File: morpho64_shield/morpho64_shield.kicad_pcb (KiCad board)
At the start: 2 copper layers, 70 x 57 mm, 13 parts, among them J1 CN7, J2 CN10, J3 Conn_Coaxial_Small, U1 ADA4505-1ARJZ-R7, U2 ADA4505-1ARJZ-R7, U3 ADA4505-1ARJZ-R7, U4 AP63203WU

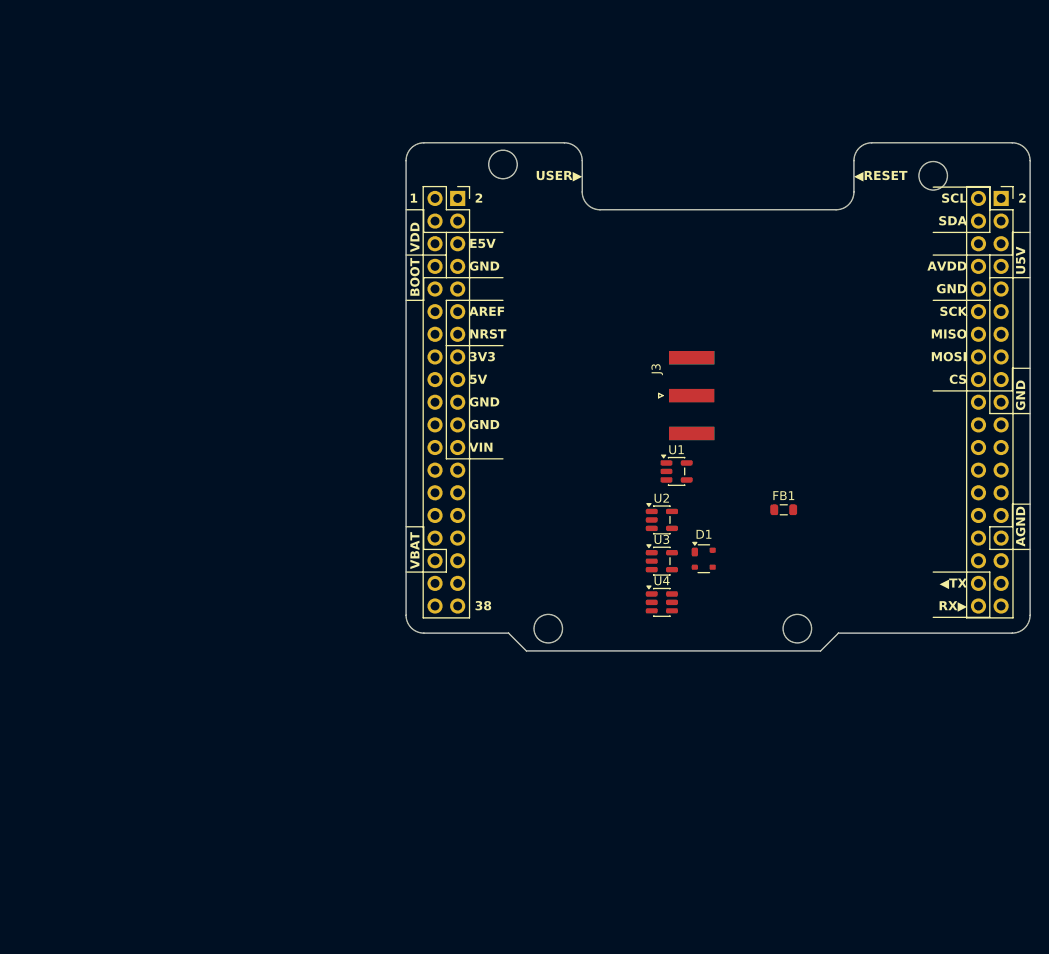
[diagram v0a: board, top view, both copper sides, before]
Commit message: esd + caps
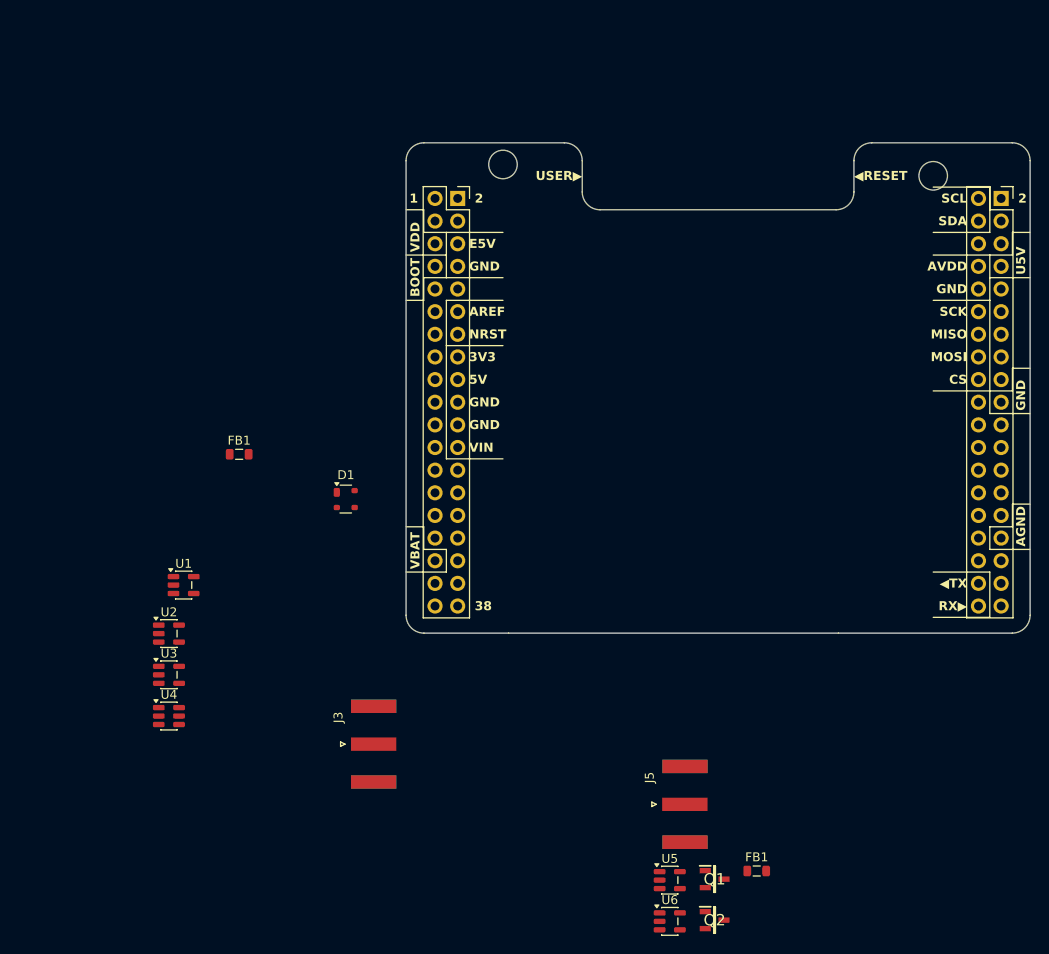
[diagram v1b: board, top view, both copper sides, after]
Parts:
- removed H1, H4: MountingHole, MountingHole:MountingHole_3.2mm_M3_ISO14580
- added FB1: FerriteBead, Inductor_SMD:L_0805_2012Metric, F.Cu at (156.7, 136.4)
- added J5: Conn_Coaxial_Small, Connector_Coaxial:SMA_Amphenol_132289_EdgeMount, F.Cu at (148.7, 128.9)
- added Q1: FMMT493TC, SamacSys_Parts:SOT95P237X112-3N, F.Cu at (152.0, 137.3)
- added Q2: FMMT593TC, SamacSys_Parts:SOT95P237X112-3N, F.Cu at (152.0, 141.9)
- added U5: OPA596DBVR, Package_TO_SOT_SMD:SOT-23-5, F.Cu at (147.0, 137.4)
- added U6: OPA596DBVR, Package_TO_SOT_SMD:SOT-23-5, F.Cu at (147.0, 142.1)
- moved FB1 61.4 mm to (98.7, 89.7)
- moved U1 56.7 mm to (92.5, 104.3)
- moved U2 56.7 mm to (90.8, 109.8)
- moved U3 56.7 mm to (90.8, 114.4)
- moved U4 56.7 mm to (90.8, 119.0)
- moved J3 52.9 mm to (113.8, 122.2)
- moved D1 40.7 mm to (110.6, 94.7)
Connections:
- net Net-(C1-Pad2) renamed /analog_input/IN_U
- net Net-(D1-I/O1) renamed /analog_input/IN_Q
- net Net-(R4-Pad2) renamed /analog_input/ADC2
- net Net-(R6-Pad2) renamed /analog_input/ADC1
- J1 pad 31: unconnected-(J1-Pin_31-Pad31) -> /shield/DAC
- J1 pad 33: unconnected-(J1-Pin_33-Pad33) -> /shield/PB0
- J1 pad 35: unconnected-(J1-Pin_35-Pad35) -> /shield/ADC2
- J1 pad 36: unconnected-(J1-Pin_36-Pad36) -> /shield/ADC2
- J1 pad 37: unconnected-(J1-Pin_37-Pad37) -> /shield/ADC1
- J2 pad 21: unconnected-(J2-Pin_21-Pad21) -> /shield/PB2
- J2 pad 23: unconnected-(J2-Pin_23-Pad23) -> /shield/PB1
- J2 pad 28: unconnected-(J2-Pin_28-Pad28) -> /shield/PB4
- J2 pad 30: unconnected-(J2-Pin_30-Pad30) -> /shield/PB5
- J2 pad 32: unconnected-(J2-Pin_32-Pad32) -> /shield/PB3
- J2 pad 4: unconnected-(J2-Pin_4-Pad4) -> /shield/PB6
- J2 pad 6: unconnected-(J2-Pin_6-Pad6) -> /shield/PB7
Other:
- board size 70 x 57 mm -> 70 x 55 mm

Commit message: First part of layout
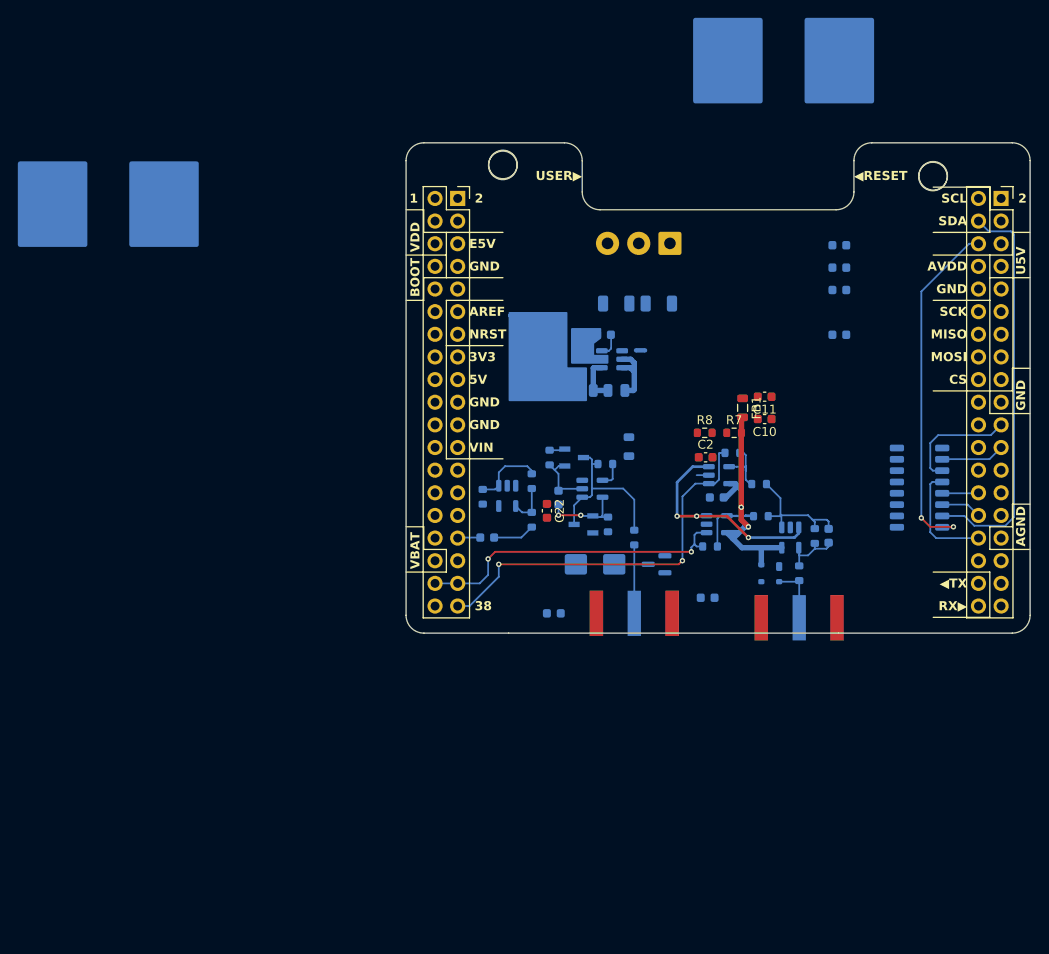
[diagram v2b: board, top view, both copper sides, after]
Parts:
- added C1: C, Capacitor_SMD:C_0603_1608Metric, B.Cu at (164.8, 98.8)
- added C10: 100nF, Capacitor_SMD:C_0603_1608Metric, F.Cu at (157.6, 85.7)
- added C11: 100nF, Capacitor_SMD:C_0603_1608Metric, F.Cu at (157.6, 83.2)
- added C12: C, Capacitor_SMD:C_0603_1608Metric, B.Cu at (126.5, 99.0)
- added C13: 100nF, Capacitor_SMD:C_0603_1608Metric, B.Cu at (166.0, 66.2)
- added C18: 100nF, Capacitor_SMD:C_0603_1608Metric, B.Cu at (166.0, 68.7)
- added C19: 100nF, Capacitor_SMD:C_0603_1608Metric, B.Cu at (166.0, 71.2)
- added C2: 100nF, Capacitor_SMD:C_0603_1608Metric, F.Cu at (151.0, 90.0)
- added C20: 100nF, Capacitor_SMD:C_0603_1608Metric, B.Cu at (152.2, 94.5)
- added C21: 100nF, Capacitor_SMD:C_0603_1608Metric, B.Cu at (166.0, 76.2)
- added C22: 100nF, Capacitor_SMD:C_0603_1608Metric, F.Cu at (133.2, 96.0)
- added C23: DNP, Capacitor_SMD:C_0603_1608Metric, B.Cu at (134.5, 94.5)
- added C24: 100nF, Capacitor_SMD:C_0603_1608Metric, B.Cu at (151.2, 105.8)
- added C25: 100nF, Capacitor_SMD:C_0603_1608Metric, B.Cu at (134.0, 107.5)
- added C3: 22uF, Capacitor_SMD:C_1206_3216Metric, B.Cu at (141.0, 72.8)
- added C4: 22uF, Capacitor_SMD:C_1206_3216Metric, B.Cu at (145.8, 72.8)
- added C5: 470uF, Capacitor_SMD:CP_Elec_16x17.5, B.Cu at (84.0, 61.6)
- added C6: 470uF, Capacitor_SMD:CP_Elec_16x17.5, B.Cu at (159.8, 45.5)
- added C7: 100nF, Capacitor_SMD:C_0603_1608Metric, B.Cu at (139.6, 76.2)
- added C8: 22uF, Capacitor_SMD:C_0805_2012Metric, B.Cu at (137.4, 82.5)
- added C9: 10uF, Capacitor_SMD:C_0805_2012Metric, B.Cu at (141.0, 82.5)
- added D2: SMBJ24CA, Diode_SMD:D_SMB, B.Cu at (138.6, 102.0)
- added D3: BAT54S, Package_TO_SOT_SMD:SOT-23, B.Cu at (145.5, 102.0)
- added H1: MountingHole, MountingHole:MountingHole_3.2mm_M3_ISO14580, B.Cu at (128.2, 57.2)
- added H4: MountingHole, MountingHole:MountingHole_3.2mm_M3_ISO14580, B.Cu at (176.5, 58.5)
- added J4: Screw_Terminal_01x03, TerminalBlock_4Ucon:TerminalBlock_4Ucon_1x03_P3.50mm_Vertical, B.Cu at (147.0, 66.0)
- added L1: 4.7uH, Inductor_SMD:L_7.3x7.3_H4.5, B.Cu at (133.7, 77.5)
- added NT1: NetTie_2, NetTie:NetTie-2_SMD_Pad0.5mm, B.Cu at (143.7, 78.0)
- added R1: R, Resistor_SMD:R_0603_1608Metric, B.Cu at (161.5, 103.0)
- added R10: R, Resistor_SMD:R_0603_1608Metric, B.Cu at (140.1, 97.5)
- added R11: R, Resistor_SMD:R_0603_1608Metric, B.Cu at (126.0, 94.4)
- added R12: R, Resistor_SMD:R_0603_1608Metric, B.Cu at (139.8, 90.8)
- added R13: R, Resistor_SMD:R_0603_1608Metric, B.Cu at (131.5, 97.0)
- added R14: R, Resistor_SMD:R_0603_1608Metric, B.Cu at (131.5, 92.7)
- added R15: DNP, Resistor_SMD:R_0603_1608Metric, B.Cu at (143.0, 99.0)
- added R2: R, Resistor_SMD:R_0603_1608Metric, B.Cu at (163.2, 98.8)
- added R3: R, Resistor_SMD:R_0603_1608Metric, B.Cu at (157.2, 96.6)
- added R4: R, Resistor_SMD:R_0603_1608Metric, B.Cu at (151.5, 100.0)
- added R5: R, Resistor_SMD:R_0603_1608Metric, B.Cu at (157.0, 93.0)
- added R6: R, Resistor_SMD:R_0603_1608Metric, B.Cu at (154.0, 89.5)
- added R7: 1k, Resistor_SMD:R_0603_1608Metric, F.Cu at (154.2, 87.2)
- added R8: 1k, Resistor_SMD:R_0603_1608Metric, F.Cu at (150.9, 87.2)
- added R9: R, Resistor_SMD:R_0603_1608Metric, B.Cu at (133.5, 90.0)
- added SW1: SW_DIP_x08, Button_Switch_SMD:SW_DIP_SPSTx08_Slide_Copal_CHS-08A_W5.08mm_P1.27mm_JPin, B.Cu at (175.0, 93.4)
- D1, FB1, J3, J5, Q1, Q2, U1, U2, U3, U4, U5, U6: moved to B.Cu
- moved U1 68.3 mm to (160.5, 99.0), turned to -90 degrees
- moved U3 65.6 mm to (152.5, 92.0)
- moved U4 63.8 mm to (140.5, 79.0), turned to 180 degrees
- moved U2 62.7 mm to (152.2, 97.5)
- moved FB1 56.7 mm to (155.2, 84.5), turned to -90 degrees
- moved U6 51.1 mm to (128.8, 94.3), turned to -90 degrees
- moved Q1 49.9 mm to (136.2, 90.0)
- moved J3 49.8 mm to (161.5, 108.0), turned to -90 degrees
- moved FB1 49.7 mm to (142.4, 88.8), turned to -90 degrees
- moved D1 48.3 mm to (158.2, 103.0), turned to 180 degrees
- moved Q2 46.8 mm to (137.3, 97.5), turned to 180 degrees
- moved U5 44.8 mm to (138.3, 93.5)
- moved J5 22.2 mm to (143.0, 107.5), turned to -90 degrees
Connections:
- J1 pad 31: /shield/DAC -> DAC_out
- J1 pad 35: /shield/ADC2 -> ADC2_in
- J1 pad 36: /shield/ADC2 -> ADC2_in
- J1 pad 37: /shield/ADC1 -> ADC1_in
- U2 pad 1: /analog_input/ADC2 -> ADC2_in
- U3 pad 1: /analog_input/ADC1 -> ADC1_in
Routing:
- net /shield/PB6: track 0.00 -> 45.2 mm
- net ADC1_in: track 0.00 -> 43.9 mm, vias 0 -> 2
- net /shield/PB7: track 0.00 -> 39.3 mm, vias 0 -> 2
- net ADC2_in: track 0.00 -> 35.8 mm, vias 0 -> 2
- net +3V3_A: track 0.00 -> 30.9 mm, vias 0 -> 2
- net +1V8_A: track 0.00 -> 24.7 mm, vias 0 -> 3
- net Net-(Q1-C): track 0.00 -> 19.0 mm
- net /analog_input/IN_U: track 0.00 -> 14.6 mm
- net /shield/PB2: track 0.00 -> 13.1 mm
- net /shield/PB3: track 0.00 -> 12.5 mm
- net Net-(D2-A2): track 0.00 -> 11.5 mm
- net Net-(U2--): track 0.00 -> 10.6 mm
- net /analog_output/U5_VCC: track 0.00 -> 9.14 mm, vias 0 -> 2
- net Net-(R11-Pad2): track 0.00 -> 8.01 mm
- net /analog_output/U5_VEE: track 0.00 -> 7.38 mm
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
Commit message: First PCB order
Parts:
- added R16: R, Resistor_SMD:R_0603_1608Metric, F.Cu at (169.5, 89.0)
- C13, C18, C19, C21, FB1, NT1: moved to F.Cu
- C5, C6: footprint Capacitor_SMD:CP_Elec_16x17.5 -> Capacitor_SMD:CP_Elec_10x7.7
- moved C5 54.8 mm to (138.5, 67.8)
- moved C21 40.0 mm to (130.3, 94.4), turned to -90 degrees
- moved C13 36.8 mm to (158.6, 102.2)
- moved C18 30.7 mm to (160.4, 99.0), turned to -90 degrees
- moved C19 29.9 mm to (152.3, 97.8), turned to 0 degrees
- moved C6 23.5 mm to (167.4, 67.7)
- moved C25 13.9 mm to (144.8, 98.8), turned to -90 degrees
- moved C11 11.2 mm to (146.6, 81.4), turned to -90 degrees
- moved C10 9.55 mm to (149.1, 81.4), turned to -90 degrees
- moved C3 8.90 mm to (149.9, 72.8)
- moved C4 8.90 mm to (154.7, 72.8)
- moved J4 8.90 mm to (155.9, 66.0)
- moved R11 8.50 mm to (134.3, 92.6), turned to 180 degrees
- moved FB1 7.32 mm to (147.8, 83.8), turned to 0 degrees
- moved FB1 6.25 mm to (147.8, 85.8), turned to 0 degrees
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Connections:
- net Net-(U4-SW) renamed /power/SW
- D3 pad 3: unconnected-(D3-COM-Pad3) -> Net-(D2-A2)
- SW1 pad 1: +3V3 -> Net-(R16-Pad2)
- SW1 pad 2: +3V3 -> Net-(R16-Pad2)
- SW1 pad 3: +3V3 -> Net-(R16-Pad2)
- SW1 pad 4: +3V3 -> Net-(R16-Pad2)
- SW1 pad 5: +3V3 -> Net-(R16-Pad2)
- SW1 pad 6: +3V3 -> Net-(R16-Pad2)
- SW1 pad 7: +3V3 -> Net-(R16-Pad2)
- SW1 pad 8: +3V3 -> Net-(R16-Pad2)
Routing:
- net -24V: track 1.75 -> 82.7 mm, vias 0 -> 3
- net +24V: track 7.17 -> 86.1 mm, vias 0 -> 5
- net /shield/PB0: track 0.00 -> 64.6 mm, vias 0 -> 1
- net +3V3: track 0.00 -> 54.4 mm, vias 0 -> 3
- net Net-(R16-Pad2): track 0.00 -> 11.0 mm, vias 0 -> 1
- net +3V3_A: track 30.9 -> 39.1 mm, vias 2 -> 4
- net +1V8_A: track 24.7 -> 32.6 mm, vias 3 -> 4
- net /power/SW: track 6.23 -> 0.67 mm
- net Net-(U5--): track 2.87 -> 8.40 mm, vias 0 -> 2
- net Net-(U2--): track 10.6 -> 7.20 mm
- net GND: track 6.50 -> 9.77 mm, vias 0 -> 82
- net /analog_input/IN_U: track 14.6 -> 16.5 mm
- net Net-(U3--): track 6.79 -> 5.50 mm
- net /power/3V3_FB: track 0.00 -> 1.18 mm, vias 0 -> 1
- net ADC2_in: track 35.8 -> 34.8 mm
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- added copper zone on B.Cu, net +3V3
- added copper zone on B.Cu, net /power/SW
- added copper zone on B.Cu, net GND
- added copper zone on F.Cu, net GND
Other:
- copper layers 2 -> 4
